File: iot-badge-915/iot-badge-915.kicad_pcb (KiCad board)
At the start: 2 copper layers, 70 x 100 mm, 74 parts, among them J1 USB_C_Receptacle_USB2.0, J2 Wire ANT, J3 Conn_01x04_Male, Q1 BC847, Q2 BC847, SW1 SW_Push, SW2 SW_Push, SW3 SW_Push, SW4 SW_Push, SW5 SW_Push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

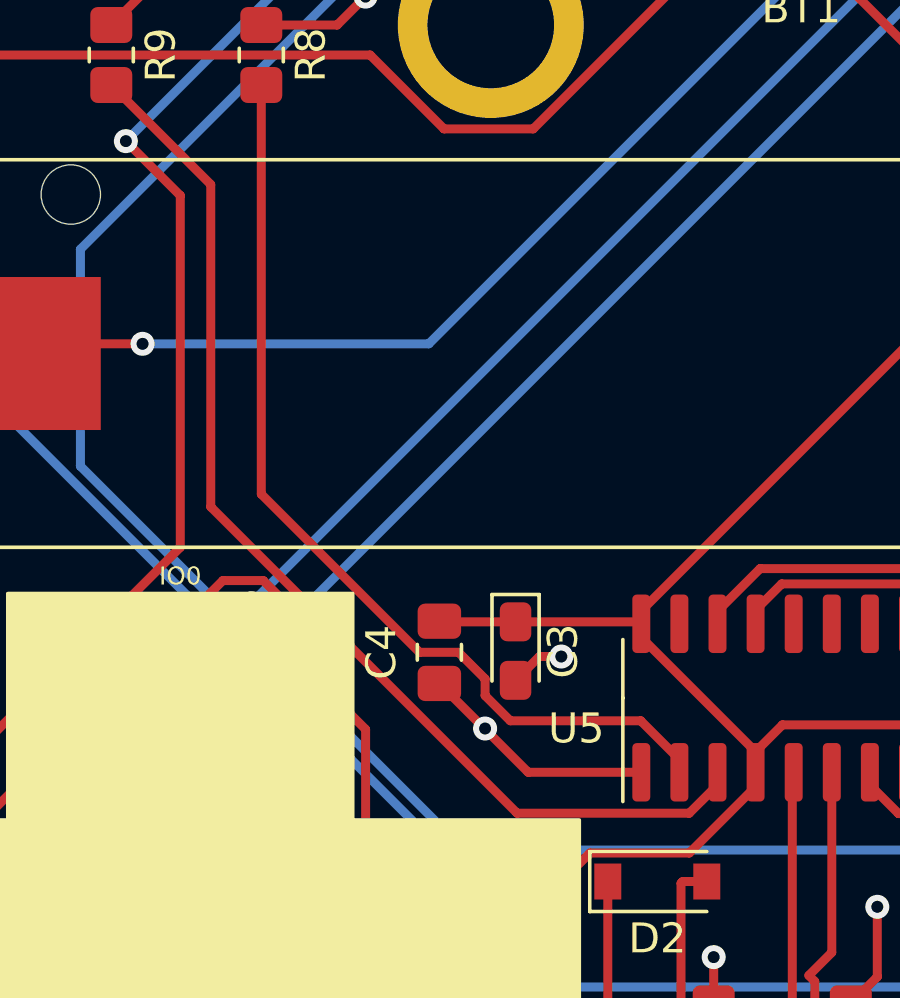
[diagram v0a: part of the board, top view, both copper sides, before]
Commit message: moved capacitors to make room
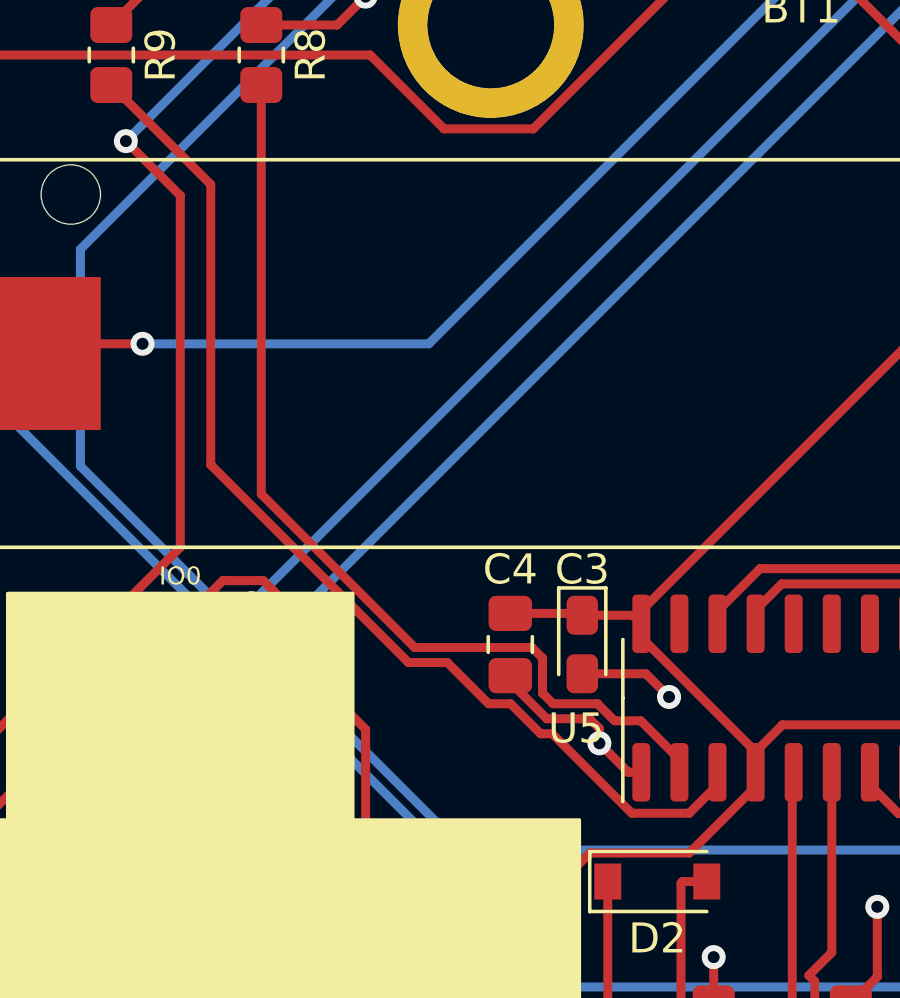
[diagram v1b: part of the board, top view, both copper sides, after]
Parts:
- moved C4 2.38 mm to (125.3, 124.2)
- moved C3 2.23 mm to (127.7, 124.2)
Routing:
- net +3.3VP: track 132.3 -> 130.1 mm
- net Net-(R9-Pad2): track 37.4 -> 36.5 mm
- net Earth: track 204.2 -> 203.5 mm

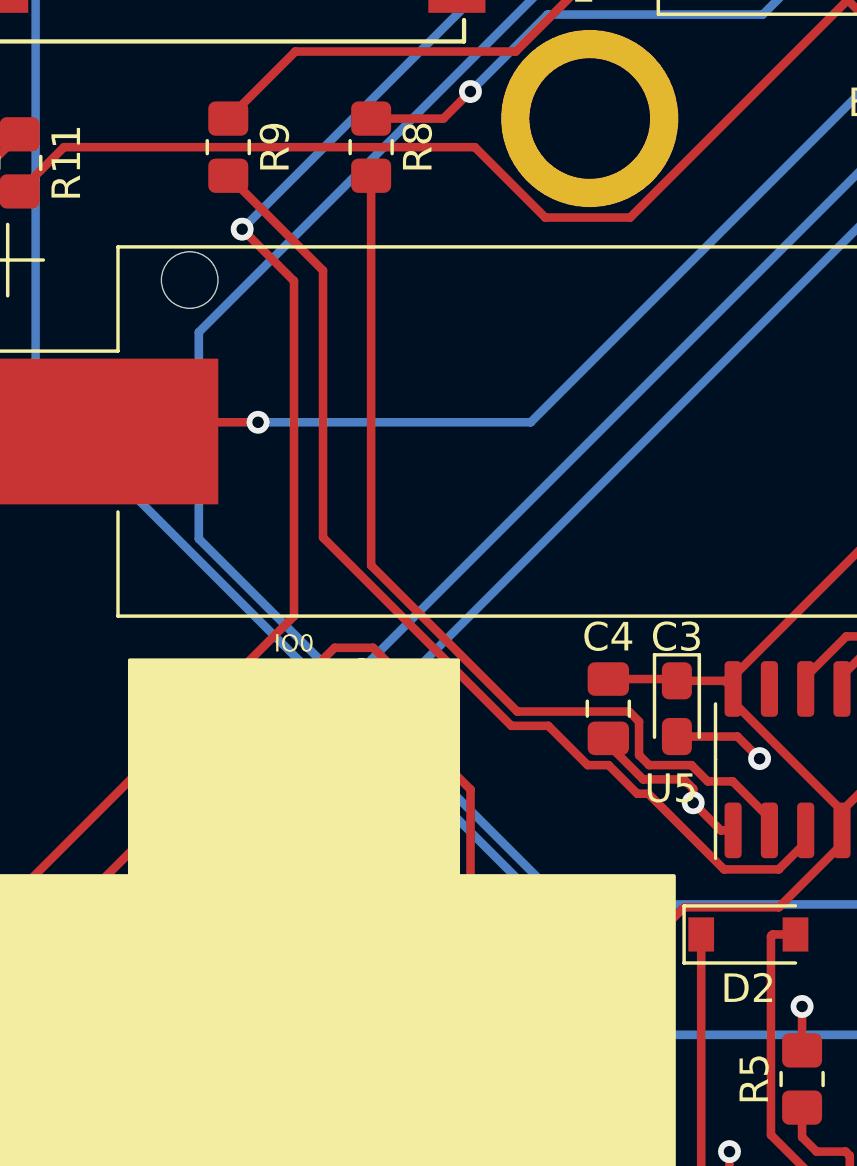
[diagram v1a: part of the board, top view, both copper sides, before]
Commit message: added resistor to switch
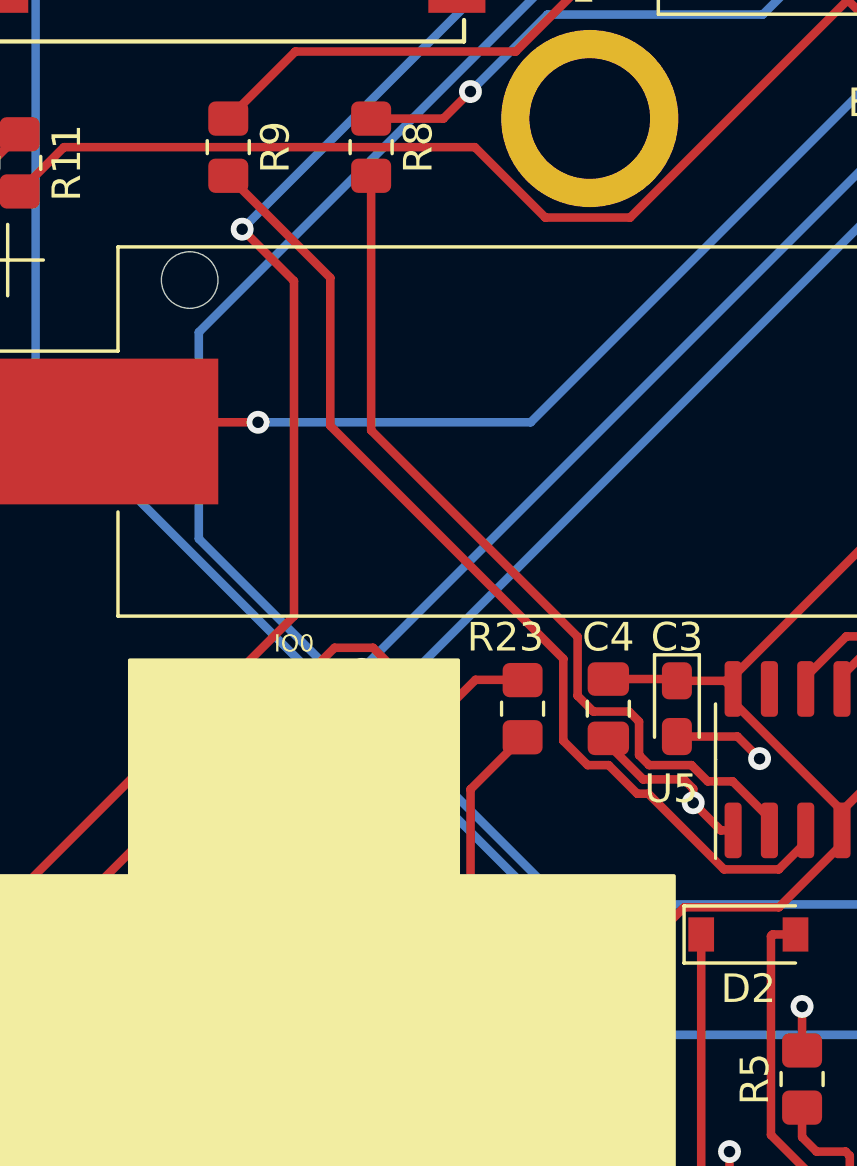
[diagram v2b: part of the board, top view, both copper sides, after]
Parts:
- added R23: 220, Resistor_SMD:R_0805_2012Metric_Pad1.20x1.40mm_HandSolder, F.Cu at (122.3, 124.2)
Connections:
- SW4 pad 1: /SW4-17 -> Net-(SW4-Pad1)
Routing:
- net Net-(SW4-Pad1): track 0.00 -> 19.8 mm
- net /SW4-17: track 94.8 -> 78.9 mm
- net Net-(R8-Pad2): track 32.4 -> 30.8 mm
- net Net-(R9-Pad2): track 36.5 -> 35.8 mm

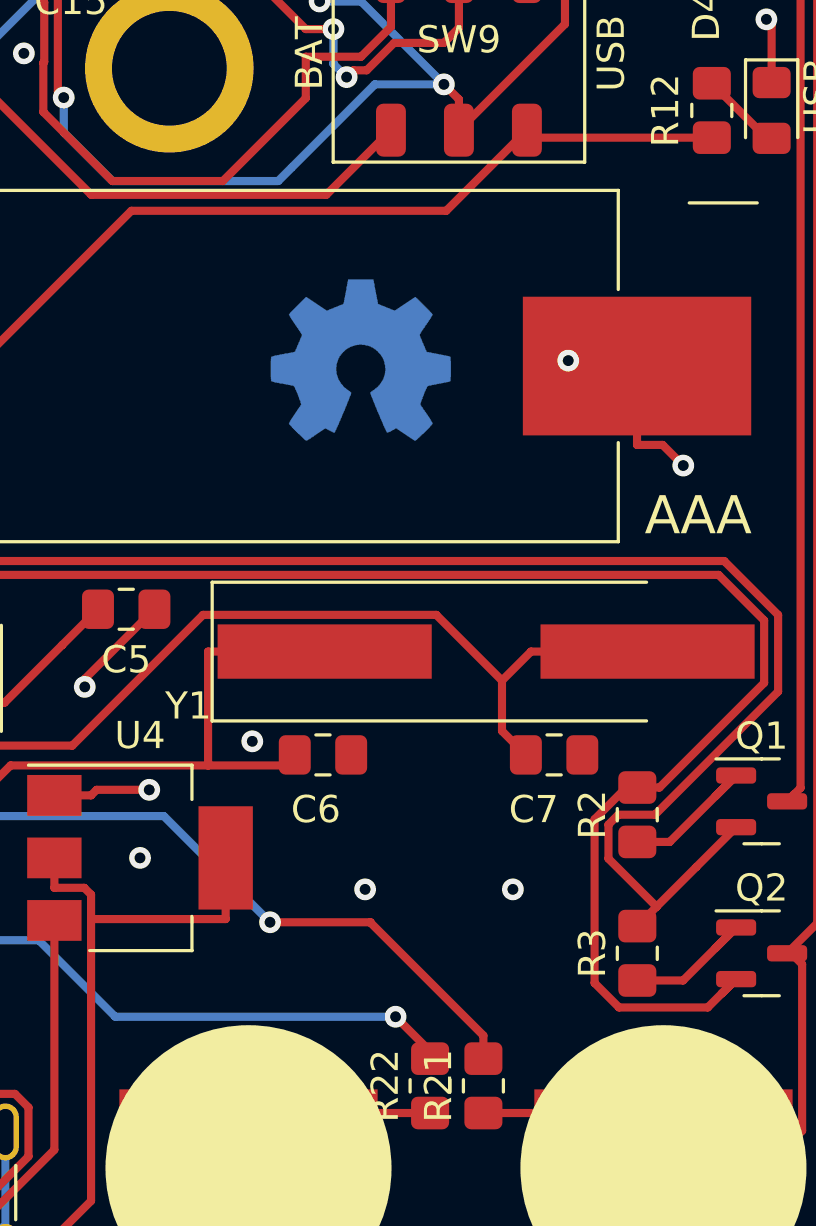
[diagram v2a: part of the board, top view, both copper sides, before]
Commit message: placed i2c mic in pcb
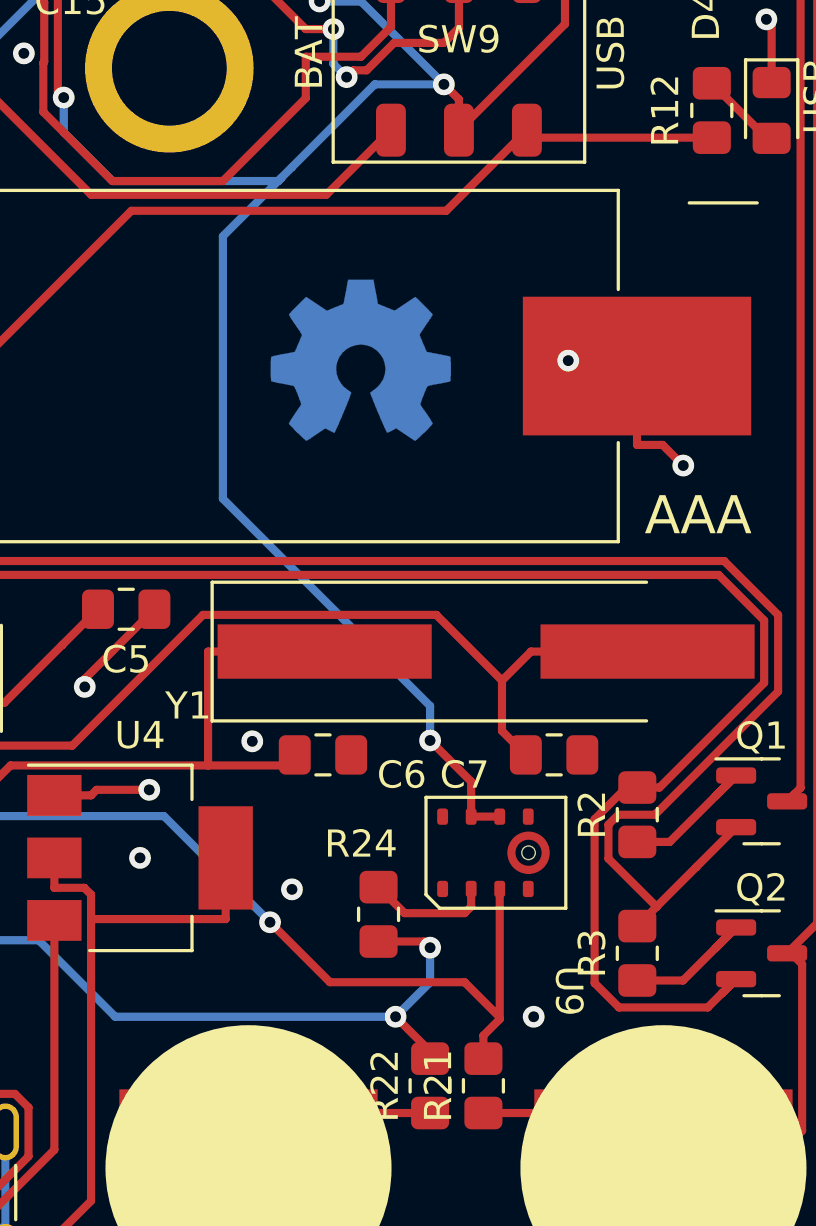
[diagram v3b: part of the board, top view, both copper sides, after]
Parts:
- added R24: 220, Resistor_SMD:R_0805_2012Metric_Pad1.20x1.40mm_HandSolder, F.Cu at (153.0, 134.7)
- added U9: INMP441, Microphone_I2S:INMP441, F.Cu at (157.5, 132.4)
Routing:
- net +3V3: track 153.5 -> 182.7 mm, vias 8 -> 9
- net /SW5-32: track 127.6 -> 133.5 mm
- net /SW6-33: track 140.3 -> 145.3 mm, vias 2 -> 3
- net Net-(U9-Pad2): track 0.00 -> 4.55 mm

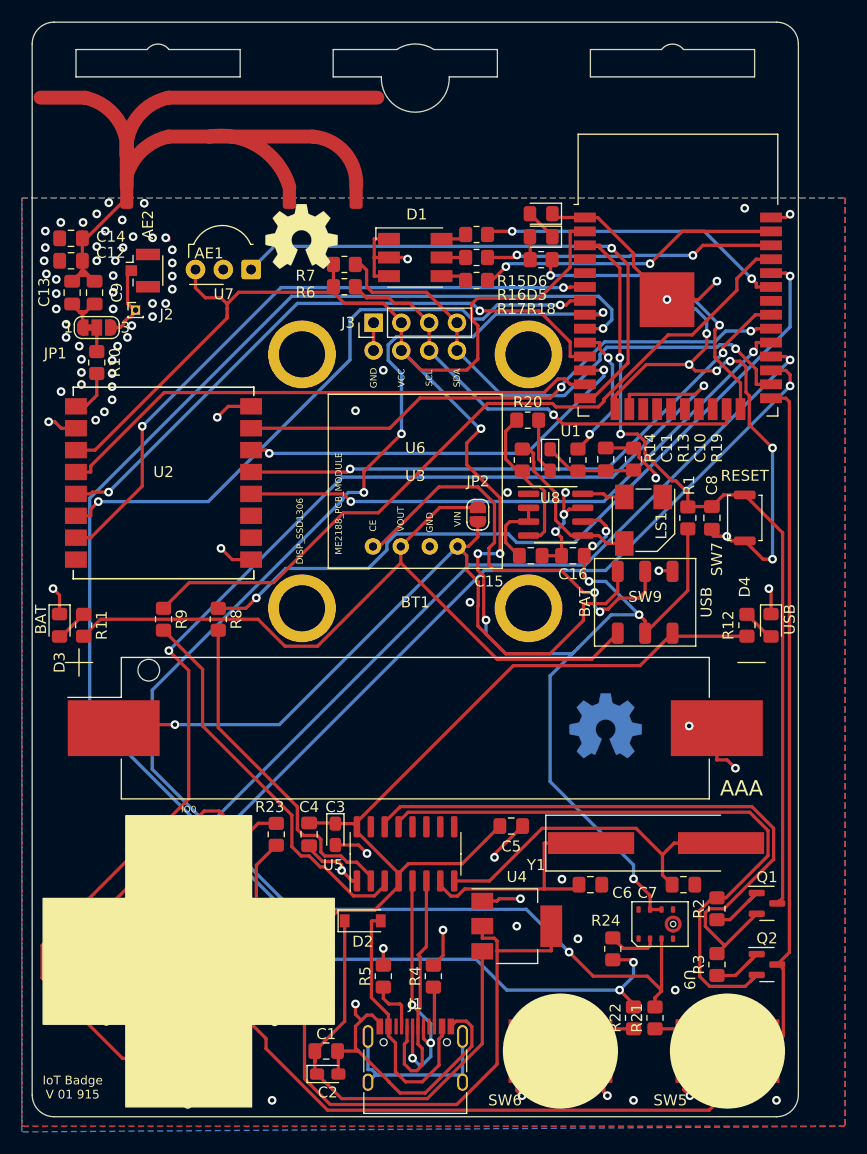
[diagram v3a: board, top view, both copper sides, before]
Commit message: finished placing i2s mic
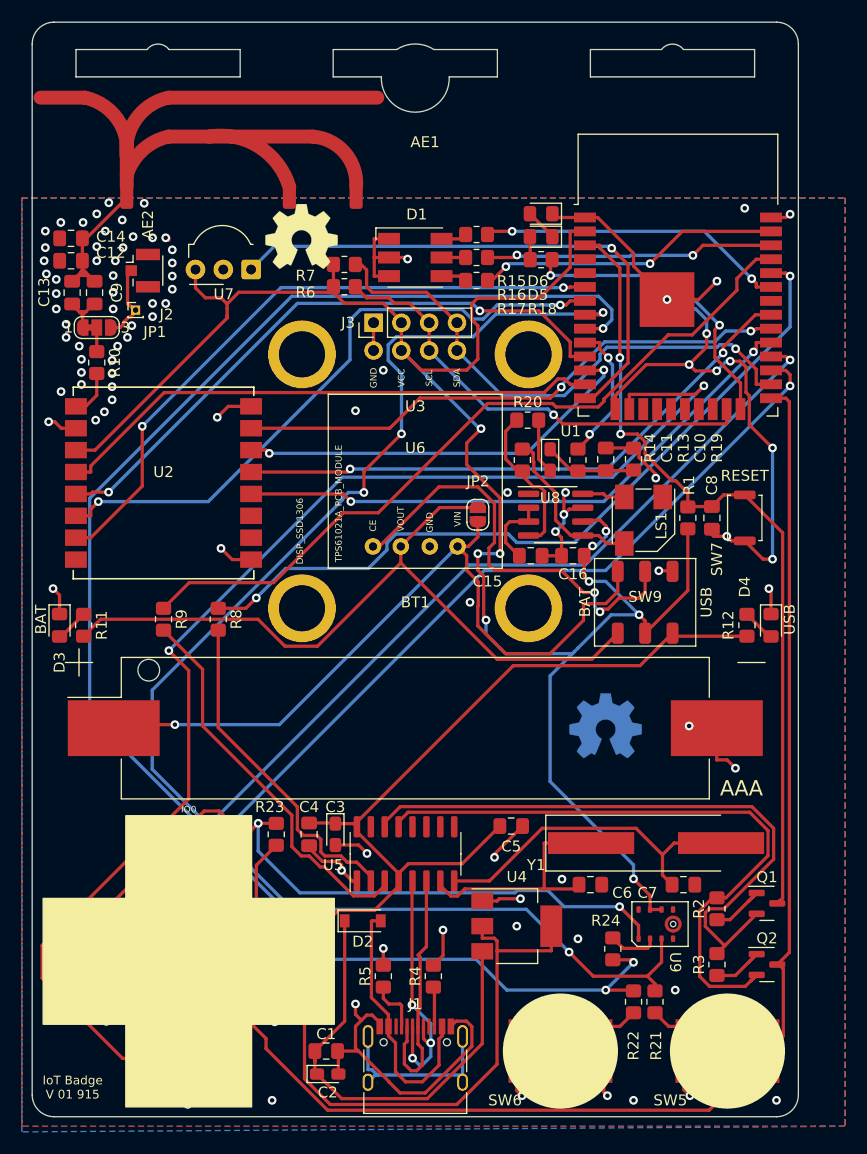
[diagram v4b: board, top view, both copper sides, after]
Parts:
- moved R21 1.47 mm to (156.9, 139.5)
- moved R22 1.47 mm to (154.9, 139.5)
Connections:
- U9 pad 1: unconnected-(U9-Pad1) -> /SW4-17
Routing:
- net /SW4-17: track 78.9 -> 120.4 mm, vias 2 -> 4
- net /SW5-32: track 133.5 -> 130.8 mm
- net Net-(R22-Pad1): track 11.4 -> 12.1 mm
- net Net-(R21-Pad1): track 10.7 -> 11.4 mm
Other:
- board text added: "TPS61021A_PCB_MODULE"
- board text removed: "ME2188_PCB_MODULE"
